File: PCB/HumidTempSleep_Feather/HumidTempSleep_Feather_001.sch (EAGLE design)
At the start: 7 parts

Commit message: Finished schematic and added PCB
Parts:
- added J5: (no value), SparkFun-Connectors:CONN_04PTH
- added R3: 10k, adafruit:R-US_R0805
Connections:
- removed net N$9: J2.10, MS2.GPIO2
- new net DATA: J2.10, J5.2, MS2.GPIO2, R3.2
- net 3V: now also J5.1, R3.1
- net GND: now also J5.4
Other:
- note added: "DHT11 Temperature Sensor"
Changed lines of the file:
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@@
 <setting verticaltext="up"/>
 </settings>
-<grid distance="0.1" unitdist="inch" unit="inch" style="lines" multiple="1" display="yes" altdistance="0.01" altunitdist="inch" altunit="inch"/>
+<grid distance="0.1" unitdist="inch" unit="inch" style="lines" multiple="1" display="no" altdistance="0.01" altunitdist="inch" altunit="inch"/>
 <layers>
 <layer number="1" name="Top" color="4" fill="1" visible="no" active="no"/>
@@
 <part name="J3" library="SparkFun-Connectors" deviceset="CONN_16" device=""/>
 <part name="J4" library="SparkFun-Connectors" deviceset="CONN_02" device=""/>
+<part name="J5" library="SparkFun-Connectors" deviceset="CONN_04" device="PTH"/>
+<part name="R3" library="adafruit" deviceset="R-US_" device="R0805" value="10k"/>
+<part name="SUPPLY3" library="supply2" library_urn="urn:adsk.eagle:library:372" deviceset="GND" device=""/>
 </parts>
 <sheets>
 <sheet>
 <plain>
+<text x="30.48" y="-20.32" size="1.778" layer="91">DHT11
+Temperature
+Sensor</text>
 </plain>
 <instances>
@@
 <attribute name="VALUE" x="63.5" y="20.066" size="1.778" layer="96" font="vector" rot="R180"/>
 <attribute name="NAME" x="63.5" y="9.652" size="1.778" layer="95" font="vector" rot="R180"/>
+</instance>
+<instance part="J5" gate="J1" x="35.56" y="-5.08" smashed="yes">
+<attribute name="VALUE" x="30.48" y="-12.446" size="1.778" layer="96" font="vector"/>
+<attribute name="NAME" x="30.48" y="3.048" size="1.778" layer="95" font="vector"/>
+</instance>
+<instance part="R3" gate="G$1" x="63.5" y="-7.62" smashed="yes" rot="R90">
+<attribute name="NAME" x="62.0014" y="-11.43" size="1.778" layer="95" rot="R90"/>
+<attribute name="VALUE" x="66.802" y="-11.43" size="1.778" layer="96" rot="R90"/>
+</instance>
+<instance part="SUPPLY3" gate="GND" x="48.26" y="7.62" smashed="yes">
+<attribute name="VALUE" x="46.355" y="4.445" size="1.778" layer="96"/>
 </instance>
 </instances>
@@
 <junction x="25.4" y="63.5"/>
 </segment>
+<segment>
+<pinref part="SUPPLY3" gate="GND" pin="GND"/>
+<wire x1="48.26" y1="10.16" x2="43.18" y2="10.16" width="0.1524" layer="91"/>
+<pinref part="J5" gate="J1" pin="4"/>
+<wire x1="40.64" y1="0" x2="43.18" y2="0" width="0.1524" layer="91"/>
+<wire x1="43.18" y1="10.16" x2="43.18" y2="0" width="0.1524" layer="91"/>
+</segment>
 </net>
 <net name="VBAT" class="0">
@@
 </segment>
 </net>
-<net name="N$9" class="0">
-<segment>
-<pinref part="J2" gate="G$1" pin="10"/>
-<pinref part="MS2" gate="G$1" pin="GPIO2"/>
-<wire x1="91.44" y1="38.1" x2="76.2" y2="38.1" width="0.1524" layer="91"/>
-</segment>
-</net>
 <net name="N$10" class="0">
 <segment>
@@
 <pinref part="MS2" gate="G$1" pin="3V"/>
 <wire x1="20.32" y1="68.58" x2="33.02" y2="68.58" width="0.1524" layer="91"/>
+<label x="25.4" y="68.58" size="1.778" layer="95"/>
+</segment>
+<segment>
+<pinref part="J5" gate="J1" pin="1"/>
+<wire x1="40.64" y1="-7.62" x2="50.8" y2="-7.62" width="0.1524" layer="91"/>
+<label x="43.18" y="-7.62" size="1.778" layer="95"/>
+<wire x1="50.8" y1="-7.62" x2="50.8" y2="-15.24" width="0.1524" layer="91"/>
+<wire x1="50.8" y1="-15.24" x2="63.5" y2="-15.24" width="0.1524" layer="91"/>
+<pinref part="R3" gate="G$1" pin="1"/>
+<wire x1="63.5" y1="-15.24" x2="63.5" y2="-12.7" width="0.1524" layer="91"/>
 </segment>
 </net>
@@
 </segment>
 </net>
+<net name="DATA" class="0">
+<segment>
+<pinref part="J5" gate="J1" pin="2"/>
+<wire x1="40.64" y1="-5.08" x2="50.8" y2="-5.08" width="0.1524" layer="91"/>
+<wire x1="50.8" y1="-5.08" x2="50.8" y2="0" width="0.1524" layer="91"/>
+<wire x1="50.8" y1="0" x2="63.5" y2="0" width="0.1524" layer="91"/>
+<pinref part="R3" gate="G$1" pin="2"/>
+<wire x1="63.5" y1="0" x2="63.5" y2="-2.54" width="0.1524" layer="91"/>
+<label x="43.18" y="-5.08" size="1.778" layer="95"/>
+<pinref part="J2" gate="G$1" pin="10"/>
+<pinref part="MS2" gate="G$1" pin="GPIO2"/>
+<wire x1="91.44" y1="38.1" x2="78.74" y2="38.1" width="0.1524" layer="91"/>
+<label x="86.36" y="38.1" size="1.778" layer="95"/>
+<wire x1="78.74" y1="38.1" x2="76.2" y2="38.1" width="0.1524" layer="91"/>
+<wire x1="63.5" y1="0" x2="78.74" y2="0" width="0.1524" layer="91"/>
+<wire x1="78.74" y1="0" x2="78.74" y2="38.1" width="0.1524" layer="91"/>
+<junction x="63.5" y="0"/>
+<junction x="78.74" y="38.1"/>
+</segment>
+</net>
 </nets>
 </sheet>
@@
 </drawing>
 <compatibility>
+<note version="6.3" minversion="6.2.2" severity="warning">
+Since Version 6.2.2 text objects can contain more than one line,
+which will not be processed correctly with this version.
+</note>
 <note version="8.2" severity="warning">
 Since Version 8.2, EAGLE supports online libraries. The ids

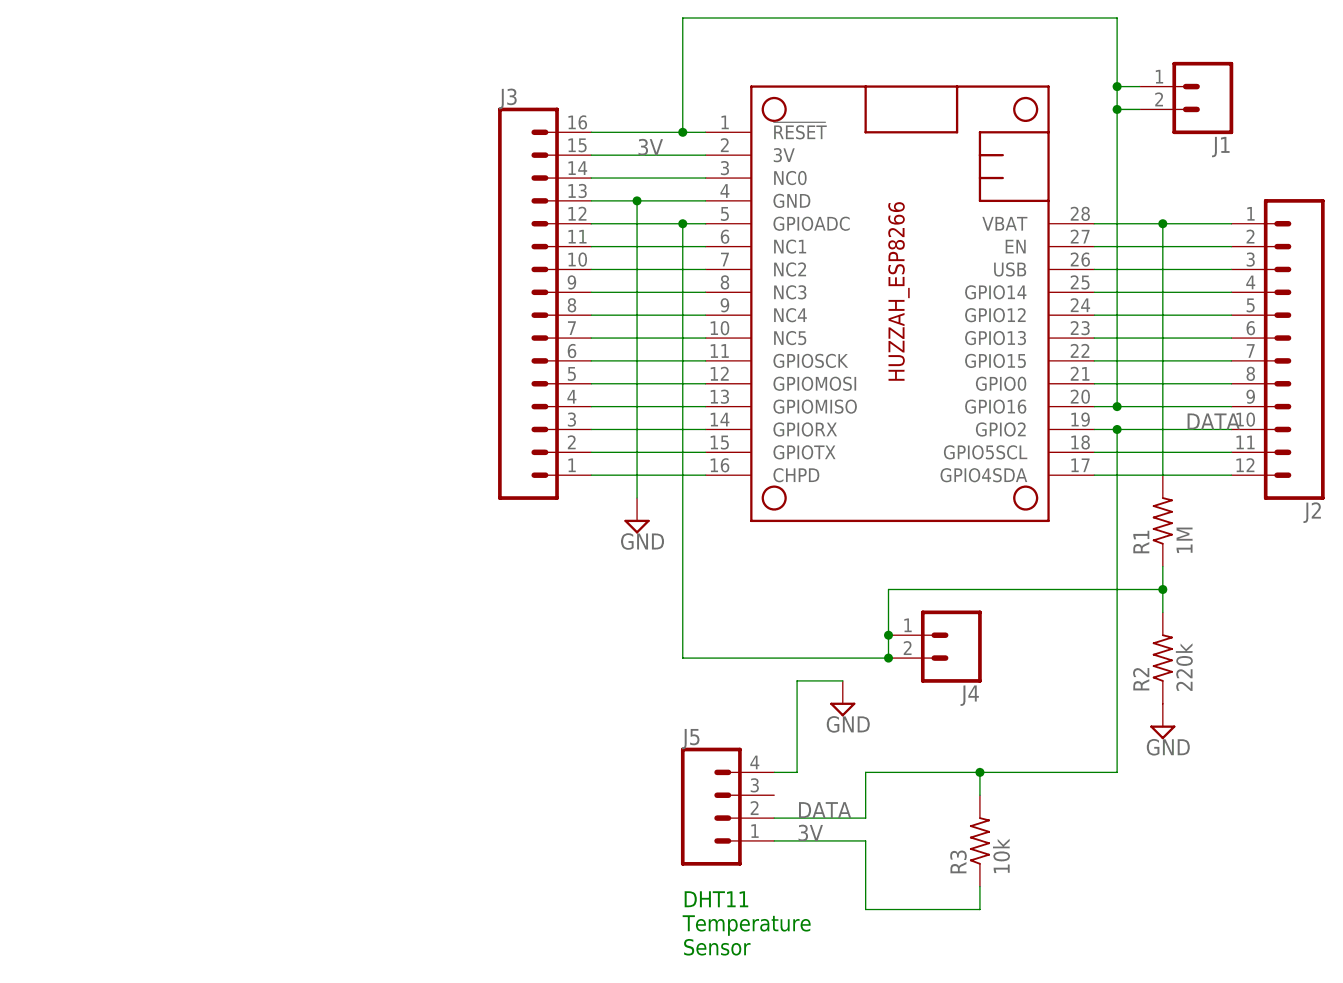
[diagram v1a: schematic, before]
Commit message: Vbatt jumper and layout
Moved the jumper for the vbatt trace, and completed most of the layout.
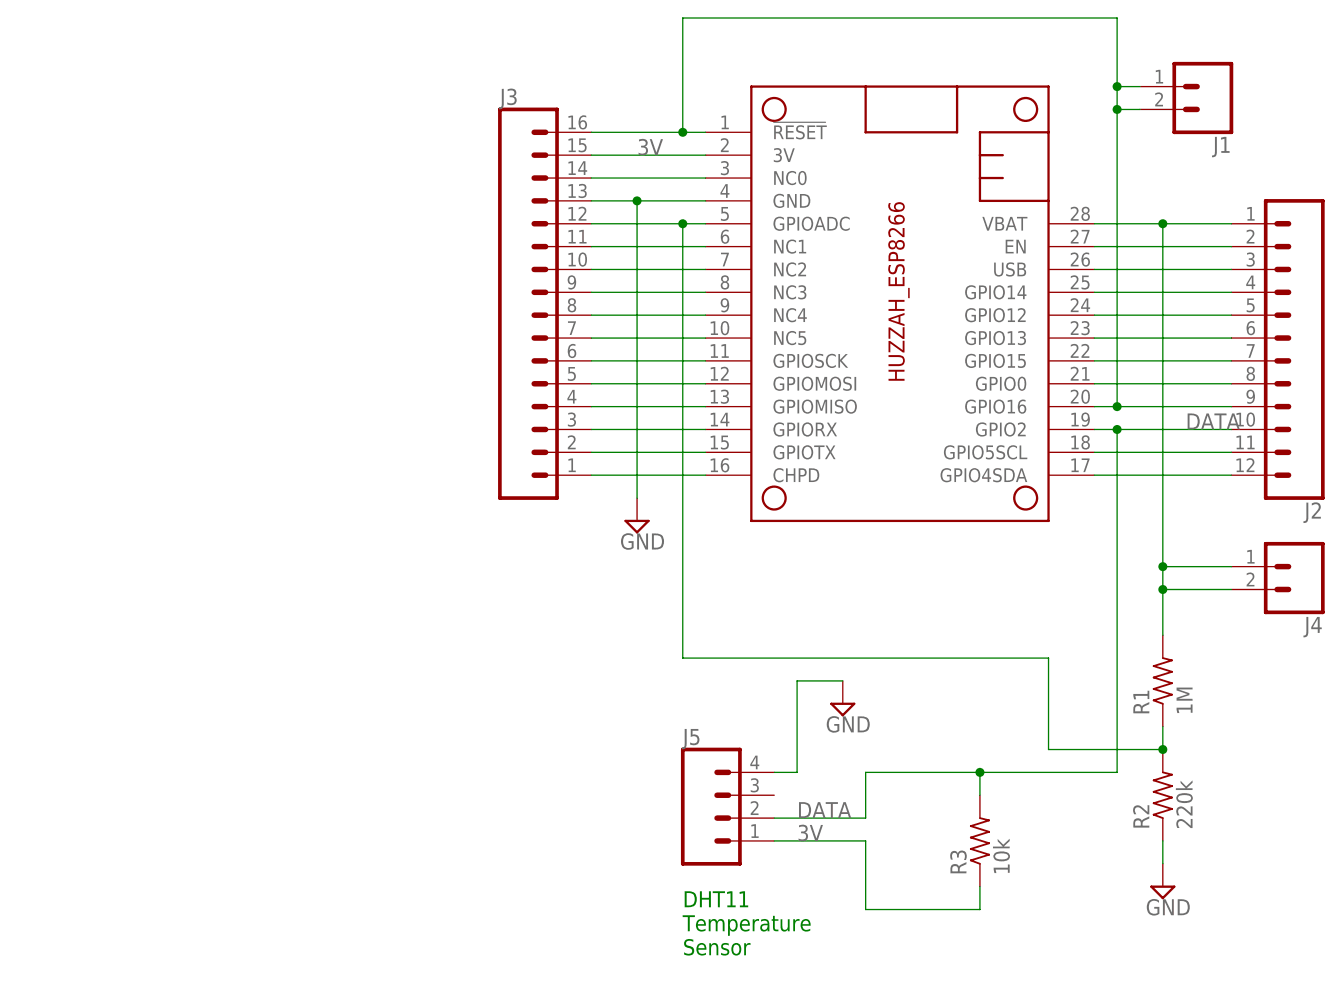
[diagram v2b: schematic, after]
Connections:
- net N$24: no longer J4.1, J4.2
- net VBAT: now also J4.1, J4.2
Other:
- moved on the sheet: J4, R1, R2
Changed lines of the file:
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@@
 </plain>
 <instances>
-<instance part="R1" gate="G$1" x="83.82" y="27.94" smashed="yes" rot="R90">
-<attribute name="NAME" x="82.3214" y="24.13" size="1.778" layer="95" rot="R90"/>
-<attribute name="VALUE" x="87.122" y="24.13" size="1.778" layer="96" rot="R90"/>
-</instance>
-<instance part="R2" gate="G$1" x="83.82" y="12.7" smashed="yes" rot="R90">
-<attribute name="NAME" x="82.3214" y="8.89" size="1.778" layer="95" rot="R90"/>
-<attribute name="VALUE" x="87.122" y="8.89" size="1.778" layer="96" rot="R90"/>
-</instance>
-<instance part="SUPPLY1" gate="GND" x="83.82" y="5.08" smashed="yes">
-<attribute name="VALUE" x="81.915" y="1.905" size="1.778" layer="96"/>
+<instance part="R1" gate="G$1" x="83.82" y="10.16" smashed="yes" rot="R90">
+<attribute name="NAME" x="82.3214" y="6.35" size="1.778" layer="95" rot="R90"/>
+<attribute name="VALUE" x="87.122" y="6.35" size="1.778" layer="96" rot="R90"/>
+</instance>
+<instance part="R2" gate="G$1" x="83.82" y="-2.54" smashed="yes" rot="R90">
+<attribute name="NAME" x="82.3214" y="-6.35" size="1.778" layer="95" rot="R90"/>
+<attribute name="VALUE" x="87.122" y="-6.35" size="1.778" layer="96" rot="R90"/>
+</instance>
+<instance part="SUPPLY1" gate="GND" x="83.82" y="-12.7" smashed="yes">
+<attribute name="VALUE" x="81.915" y="-15.875" size="1.778" layer="96"/>
 </instance>
 <instance part="SUPPLY2" gate="GND" x="25.4" y="27.94" smashed="yes">
@@
 <attribute name="NAME" x="10.16" y="74.168" size="1.778" layer="95" font="vector"/>
 </instance>
-<instance part="J4" gate="G$1" x="60.96" y="15.24" smashed="yes" rot="R180">
-<attribute name="VALUE" x="63.5" y="20.066" size="1.778" layer="96" font="vector" rot="R180"/>
-<attribute name="NAME" x="63.5" y="9.652" size="1.778" layer="95" font="vector" rot="R180"/>
+<instance part="J4" gate="G$1" x="99.06" y="22.86" smashed="yes" rot="R180">
+<attribute name="VALUE" x="101.6" y="27.686" size="1.778" layer="96" font="vector" rot="R180"/>
+<attribute name="NAME" x="101.6" y="17.272" size="1.778" layer="95" font="vector" rot="R180"/>
 </instance>
 <instance part="J5" gate="J1" x="35.56" y="-5.08" smashed="yes">
@@
 <pinref part="SUPPLY1" gate="GND" pin="GND"/>
 <pinref part="R2" gate="G$1" pin="1"/>
+<wire x1="83.82" y1="-7.62" x2="83.82" y2="-10.16" width="0.1524" layer="91"/>
 </segment>
 <segment>
@@
 <net name="VBAT" class="0">
 <segment>
-<wire x1="76.2" y1="60.96" x2="83.82" y2="60.96" width="0.1524" layer="91"/>
-<pinref part="R1" gate="G$1" pin="2"/>
-<wire x1="83.82" y1="60.96" x2="83.82" y2="33.02" width="0.1524" layer="91"/>
 <pinref part="MS2" gate="G$1" pin="VBAT"/>
 <pinref part="J2" gate="G$1" pin="1"/>
+<wire x1="76.2" y1="60.96" x2="83.82" y2="60.96" width="0.1524" layer="91"/>
+<pinref part="J4" gate="G$1" pin="1"/>
 <wire x1="83.82" y1="60.96" x2="91.44" y2="60.96" width="0.1524" layer="91"/>
+<wire x1="83.82" y1="60.96" x2="83.82" y2="22.86" width="0.1524" layer="91"/>
+<wire x1="83.82" y1="22.86" x2="91.44" y2="22.86" width="0.1524" layer="91"/>
 <junction x="83.82" y="60.96"/>
+<pinref part="J4" gate="G$1" pin="2"/>
+<wire x1="91.44" y1="20.32" x2="83.82" y2="20.32" width="0.1524" layer="91"/>
+<pinref part="R1" gate="G$1" pin="2"/>
+<wire x1="83.82" y1="20.32" x2="83.82" y2="15.24" width="0.1524" layer="91"/>
+<wire x1="83.82" y1="22.86" x2="83.82" y2="20.32" width="0.1524" layer="91"/>
+<junction x="83.82" y="22.86"/>
+<junction x="83.82" y="20.32"/>
 </segment>
 </net>
@@
 <net name="N$24" class="0">
 <segment>
-<pinref part="R2" gate="G$1" pin="2"/>
-<pinref part="R1" gate="G$1" pin="1"/>
-<wire x1="83.82" y1="22.86" x2="83.82" y2="20.32" width="0.1524" layer="91"/>
-<wire x1="83.82" y1="20.32" x2="83.82" y2="17.78" width="0.1524" layer="91"/>
-<wire x1="83.82" y1="20.32" x2="53.34" y2="20.32" width="0.1524" layer="91"/>
-<junction x="83.82" y="20.32"/>
-<pinref part="J4" gate="G$1" pin="1"/>
-<wire x1="53.34" y1="20.32" x2="53.34" y2="15.24" width="0.1524" layer="91"/>
 <wire x1="33.02" y1="60.96" x2="30.48" y2="60.96" width="0.1524" layer="91"/>
 <wire x1="30.48" y1="60.96" x2="30.48" y2="12.7" width="0.1524" layer="91"/>
@@
 <wire x1="30.48" y1="60.96" x2="20.32" y2="60.96" width="0.1524" layer="91"/>
 <junction x="30.48" y="60.96"/>
-<pinref part="J4" gate="G$1" pin="2"/>
-<wire x1="53.34" y1="12.7" x2="30.48" y2="12.7" width="0.1524" layer="91"/>
-<wire x1="53.34" y1="15.24" x2="53.34" y2="12.7" width="0.1524" layer="91"/>
-<junction x="53.34" y="15.24"/>
-<junction x="53.34" y="12.7"/>
-</segment>
-</net>
+<wire x1="30.48" y1="12.7" x2="71.12" y2="12.7" width="0.1524" layer="91"/>
+<wire x1="71.12" y1="12.7" x2="71.12" y2="2.54" width="0.1524" layer="91"/>
+<pinref part="R2" gate="G$1" pin="2"/>
+<pinref part="R1" gate="G$1" pin="1"/>
+<wire x1="83.82" y1="2.54" x2="83.82" y2="5.08" width="0.1524" layer="91"/>
+<wire x1="71.12" y1="2.54" x2="83.82" y2="2.54" width="0.1524" layer="91"/>
+<junction x="83.82" y="2.54"/>
+</segment>
+</net>

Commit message: Added prototype jumpers
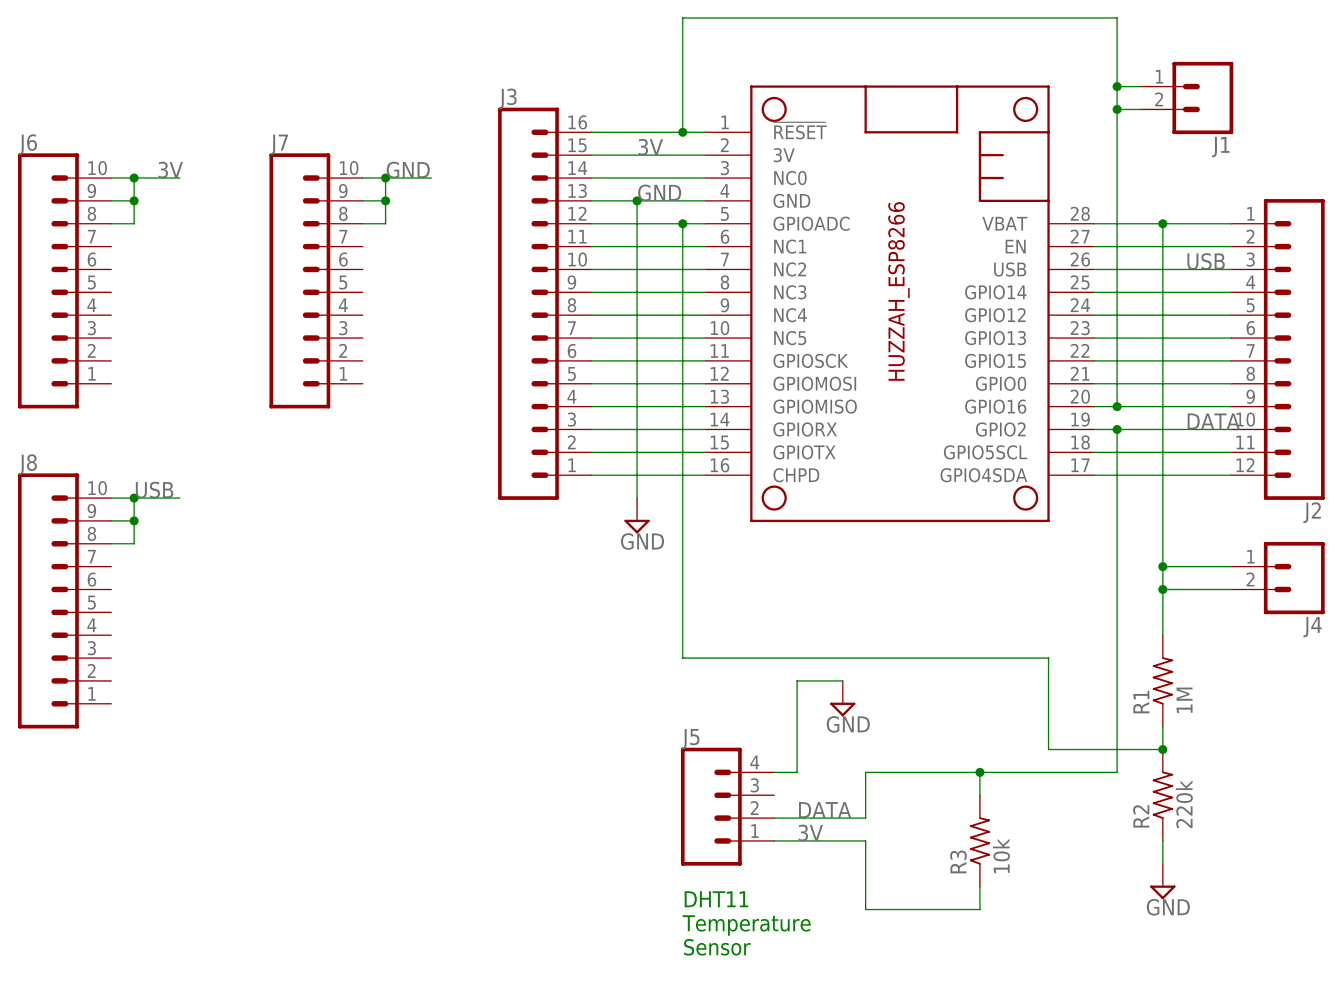
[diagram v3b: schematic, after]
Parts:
- added J6, J7, J8: (no value), SparkFun-Connectors:CONN_10"
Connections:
- net 3V: now also J6.10, J6.8, J6.9
- net GND: now also J7.10, J7.8, J7.9
- net USB: now also J8.10, J8.8, J8.9
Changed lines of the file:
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@@
 <part name="R3" library="adafruit" deviceset="R-US_" device="R0805" value="10k"/>
 <part name="SUPPLY3" library="supply2" library_urn="urn:adsk.eagle:library:372" deviceset="GND" device=""/>
+<part name="J6" library="SparkFun-Connectors" deviceset="CONN_10" device="&quot;"/>
+<part name="J7" library="SparkFun-Connectors" deviceset="CONN_10" device="&quot;"/>
+<part name="J8" library="SparkFun-Connectors" deviceset="CONN_10" device="&quot;"/>
 </parts>
 <sheets>
@@
 <instance part="SUPPLY3" gate="GND" x="48.26" y="7.62" smashed="yes">
 <attribute name="VALUE" x="46.355" y="4.445" size="1.778" layer="96"/>
+</instance>
+<instance part="J6" gate="J1" x="-43.18" y="60.96" smashed="yes">
+<attribute name="VALUE" x="-43.18" y="38.354" size="1.778" layer="96" font="vector"/>
+<attribute name="NAME" x="-43.18" y="69.088" size="1.778" layer="95" font="vector"/>
+</instance>
+<instance part="J7" gate="J1" x="-15.24" y="60.96" smashed="yes">
+<attribute name="VALUE" x="-15.24" y="38.354" size="1.778" layer="96" font="vector"/>
+<attribute name="NAME" x="-15.24" y="69.088" size="1.778" layer="95" font="vector"/>
+</instance>
+<instance part="J8" gate="J1" x="-43.18" y="25.4" smashed="yes">
+<attribute name="VALUE" x="-43.18" y="2.794" size="1.778" layer="96" font="vector"/>
+<attribute name="NAME" x="-43.18" y="33.528" size="1.778" layer="95" font="vector"/>
 </instance>
 </instances>
@@
 <wire x1="20.32" y1="63.5" x2="25.4" y2="63.5" width="0.1524" layer="91"/>
 <junction x="25.4" y="63.5"/>
+<label x="25.4" y="63.5" size="1.778" layer="95"/>
 </segment>
 <segment>
@@
 <wire x1="40.64" y1="0" x2="43.18" y2="0" width="0.1524" layer="91"/>
 <wire x1="43.18" y1="10.16" x2="43.18" y2="0" width="0.1524" layer="91"/>
+</segment>
+<segment>
+<pinref part="J7" gate="J1" pin="10"/>
+<wire x1="-5.08" y1="66.04" x2="-2.54" y2="66.04" width="0.1524" layer="91"/>
+<wire x1="-2.54" y1="66.04" x2="-2.54" y2="63.5" width="0.1524" layer="91"/>
+<pinref part="J7" gate="J1" pin="8"/>
+<wire x1="-2.54" y1="63.5" x2="-2.54" y2="60.96" width="0.1524" layer="91"/>
+<wire x1="-2.54" y1="60.96" x2="-5.08" y2="60.96" width="0.1524" layer="91"/>
+<pinref part="J7" gate="J1" pin="9"/>
+<wire x1="-5.08" y1="63.5" x2="-2.54" y2="63.5" width="0.1524" layer="91"/>
+<junction x="-2.54" y="63.5"/>
+<junction x="-2.54" y="66.04"/>
+<wire x1="-2.54" y1="66.04" x2="2.54" y2="66.04" width="0.1524" layer="91"/>
+<label x="-2.54" y="66.04" size="1.778" layer="95"/>
 </segment>
 </net>
@@
 <pinref part="J2" gate="G$1" pin="3"/>
 <wire x1="76.2" y1="55.88" x2="91.44" y2="55.88" width="0.1524" layer="91"/>
+<label x="86.36" y="55.88" size="1.778" layer="95"/>
+</segment>
+<segment>
+<pinref part="J8" gate="J1" pin="10"/>
+<wire x1="-33.02" y1="30.48" x2="-30.48" y2="30.48" width="0.1524" layer="91"/>
+<pinref part="J8" gate="J1" pin="9"/>
+<wire x1="-30.48" y1="30.48" x2="-30.48" y2="27.94" width="0.1524" layer="91"/>
+<wire x1="-30.48" y1="27.94" x2="-33.02" y2="27.94" width="0.1524" layer="91"/>
+<wire x1="-30.48" y1="27.94" x2="-30.48" y2="25.4" width="0.1524" layer="91"/>
+<junction x="-30.48" y="27.94"/>
+<pinref part="J8" gate="J1" pin="8"/>
+<wire x1="-30.48" y1="25.4" x2="-33.02" y2="25.4" width="0.1524" layer="91"/>
+<wire x1="-30.48" y1="30.48" x2="-25.4" y2="30.48" width="0.1524" layer="91"/>
+<junction x="-30.48" y="30.48"/>
+<label x="-30.48" y="30.48" size="1.778" layer="95"/>
 </segment>
 </net>
@@
 <wire x1="63.5" y1="-15.24" x2="63.5" y2="-12.7" width="0.1524" layer="91"/>
 </segment>
-</net>
+<segment>
+<pinref part="J6" gate="J1" pin="10"/>
+<wire x1="-33.02" y1="66.04" x2="-30.48" y2="66.04" width="0.1524" layer="91"/>
+<wire x1="-30.48" y1="66.04" x2="-30.48" y2="63.5" width="0.1524" layer="91"/>
+<pinref part="J6" gate="J1" pin="8"/>
+<wire x1="-30.48" y1="63.5" x2="-30.48" y2="60.96" width="0.1524" layer="91"/>
+<wire x1="-30.48" y1="60.96" x2="-33.02" y2="60.96" width="0.1524" layer="91"/>
+<pinref part="J6" gate="J1" pin="9"/>
+<wire x1="-33.02" y1="63.5" x2="-30.48" y2="63.5" width="0.1524" layer="91"/>
+<junction x="-30.48" y="63.5"/>
+<junction x="-30.48" y="66.04"/>
+<wire x1="-30.48" y1="66.04" x2="-25.4" y2="66.04" width="0.1524" layer="91"/>
+<label x="-27.94" y="66.04" size="1.778" layer="95"/>
+</segment>
+</net>
